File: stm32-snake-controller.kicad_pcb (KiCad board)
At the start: 4 copper layers, 98 x 72 mm, 72 parts, among them J101 Barrel_Jack_MountingPin, J102 JST 2.54 Header, J103 Tag Connector, J301 Conn_01x03, J302 Conn_01x03, J401 Conn_01x07, J402 Conn_01x07, J501 USB_A, Q101 AO3501A, SW101 SW_Push, U101 USBLC6-2SC6, U102 M24C64-RMN, U103 STM32F446RCTx, U201 XC6220B331MR-G, U301 74AHCT1G125, U302 74AHCT1G125, U501 STMPS2141STR, Y101 32.768kHz, Y102 16MHz

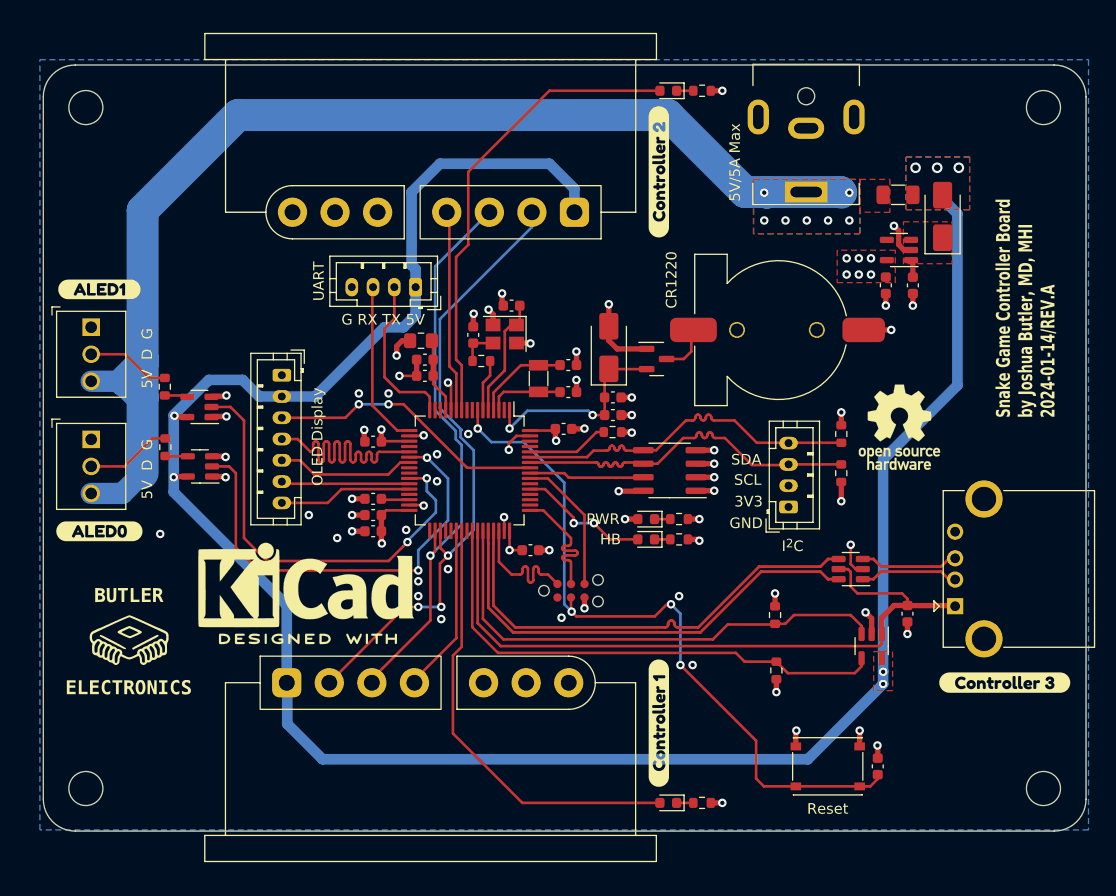
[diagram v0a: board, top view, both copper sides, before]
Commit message: update schematic and pcb design to rev-b
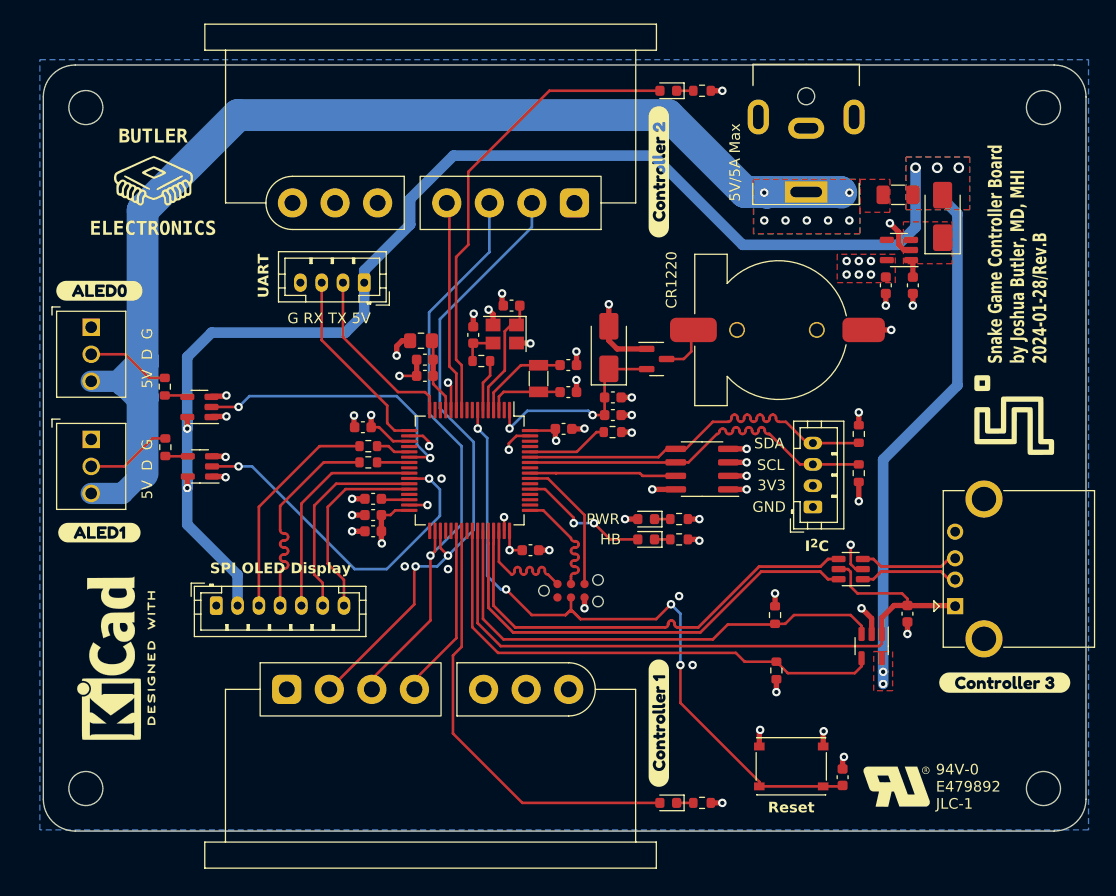
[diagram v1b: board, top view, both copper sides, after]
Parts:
- removed the REF** at (163.7, 112.8)
- removed the REF** at (219.5, 98.0)
- added G***: LOGO, LOGO, F.Cu at (219.2, 131.8)
- added G***: LOGO, LOGO, F.Cu at (230.3, 96.9)
- added R109: 47, Resistor_SMD:R_0603_1608Metric, F.Cu at (169.5, 99.8)
- added R110: 47, Resistor_SMD:R_0603_1608Metric, F.Cu at (169.5, 101.3)
- added REF**: KiCad-Logo2_6mm_SilkScreen, Symbol:KiCad-Logo2_6mm_SilkScreen, F.Cu at (145.2, 119.8)
- D103: value GREEN -> YELLOW
- D104, D105: value GREEN -> BLUE
- moved G*** 43.2 mm to (149.4, 74.9)
- moved kibuzzard-65A37F1A 22.9 mm to (144.3, 108.0)
- moved kibuzzard-65A37F11 22.6 mm to (144.3, 85.2)
- moved OLED102 22.5 mm to (155.3, 114.8), turned to 0 degrees
- moved J102 4.84 mm to (169.2, 84.5)
- moved C110 3.46 mm to (214.1, 130.9)
- moved SW101 3.43 mm to (209.3, 129.9)
- moved U102 3.05 mm to (200.9, 102.0)
- moved OLED101 2.29 mm to (211.3, 105.5)
- moved C104 1.66 mm to (169.0, 98.0)
- moved R107 1.65 mm to (215.6, 98.7)
- moved R108 1.65 mm to (215.6, 102.4)
- moved J402 0.88 mm to (175.3, 77.0)
- moved J401 0.62 mm to (175.5, 122.7)
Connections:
- J401 pad 1: +5V -> +3V3
- J402 pad 1: +5V -> +3V3
- OLED102 pad 3: /MOSI -> Net-(OLED102-SCLK)
- OLED102 pad 4: /SPI_CLK -> Net-(OLED102-MOSI)
- U103 pad 23: /OLED_RST -> /MOSI
- U103 pad 25: unconnected-(U103-PC5-Pad25) -> /OLED_RST
- U103 pad 57: /MOSI -> unconnected-(U103-PB5-Pad57)
- U301 pad 2: /LED_GRID1 -> /LED_GRID0
- U302 pad 2: /LED_GRID0 -> /LED_GRID1
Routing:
- net +5V: track 205.0 -> 169.1 mm
- net /SPI_CLK: track 29.2 -> 3.25 mm
- net /MOSI: track 26.3 -> 3.03 mm, vias 2 -> 0
- net Net-(OLED102-MOSI): track 0.00 -> 21.2 mm
- net Net-(OLED102-SCLK): track 0.00 -> 21.1 mm
- net /LED_GRID0: track 41.8 -> 26.9 mm
- net /OLED_RST: track 13.0 -> 20.9 mm
- net /LED_GRID1: track 40.7 -> 33.3 mm
- net /OLED_CE: track 12.1 -> 19.5 mm
- net /OLED_DC: track 12.5 -> 18.3 mm
- net /~{EEPROM}: track 10.8 -> 13.8 mm
- net /UART_RX: track 15.6 -> 18.1 mm
- net /SDA: track 33.8 -> 36.2 mm
- net /SCL: track 33.8 -> 35.8 mm
- net /SNES_LATCH: track 53.4 -> 55.3 mm
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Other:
- board text added: "${TITLE} by ${COMMENT1} ${ISSUE_DATE}/Rev.${REVISION}"
- board text added: "94V-0 E479892 JLC-1"
- board text added: "SPI OLED Display"
- board text removed: "${TITLE} by ${COMMENT1} ${ISSUE_DATE}/REV.${REVISION}"
- board text removed: "OLED Display"

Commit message: add power switch, rearrange pins for OLED display
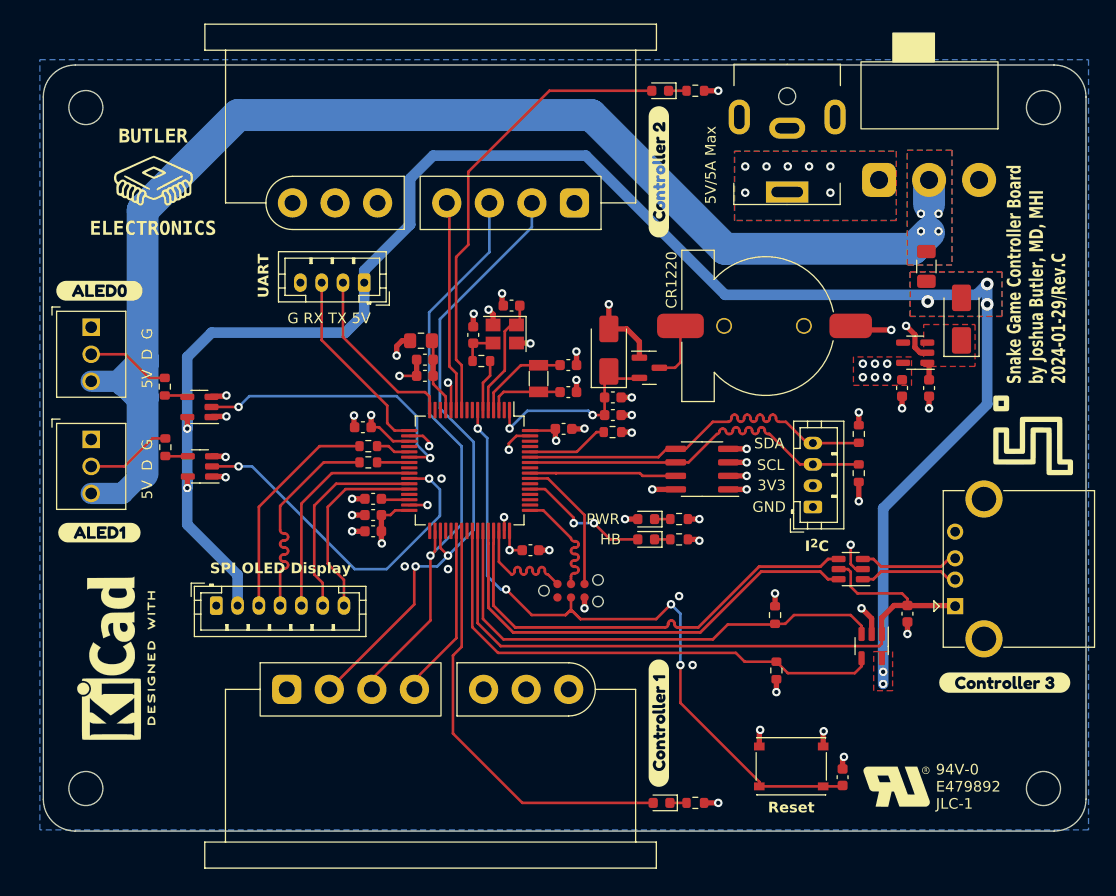
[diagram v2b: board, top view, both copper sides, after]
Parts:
- added SW102: SW_SPDT, User_Footprint:Slide_Switch_SPDT_SS-12D06L5, F.Cu at (222.2, 74.8)
- moved D101 9.81 mm to (225.3, 87.9)
- moved C201 9.77 mm to (222.2, 94.4)
- moved C202 9.77 mm to (219.7, 94.4)
- moved U201 9.77 mm to (220.9, 91.0)
- moved F101 7.24 mm to (222.0, 82.9), turned to -90 degrees
- moved G*** 2.61 mm to (232.0, 98.8)
- moved J101 1.78 mm to (208.9, 80.9)
- moved BT101 1.28 mm to (206.9, 88.5)
- moved Q101 1.07 mm to (196.0, 92.5)
- moved D104 0.76 mm to (197.0, 66.4)
- moved R103 0.63 mm to (200.3, 66.4)
- moved R104 0.63 mm to (200.3, 133.3)
- moved D105 0.63 mm to (197.1, 133.3)
- moved D102 0.25 mm to (192.2, 90.8)
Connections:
- J101 pad 1: VBUS -> Net-(SW102-A)
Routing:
- net VBUS: track 111.1 -> 124.1 mm, vias 7 -> 4
- net +5V: track 169.1 -> 165.2 mm
- net /BAT+: track 4.72 -> 5.62 mm
- net /LED_SNES1: track 44.2 -> 43.5 mm
- net /VBAT: track 19.6 -> 19.0 mm
- net /LED_SNES0: track 41.5 -> 40.9 mm
- net GND: track 69.0 -> 69.5 mm
- net Net-(SW102-A): vias 0 -> 7
- added copper zone on B.Cu, net Net-(SW102-A)
- added copper zone on F.Cu, net Net-(SW102-A)

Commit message: add scoreboard connector
- add ethernet jack for scoreboard connection
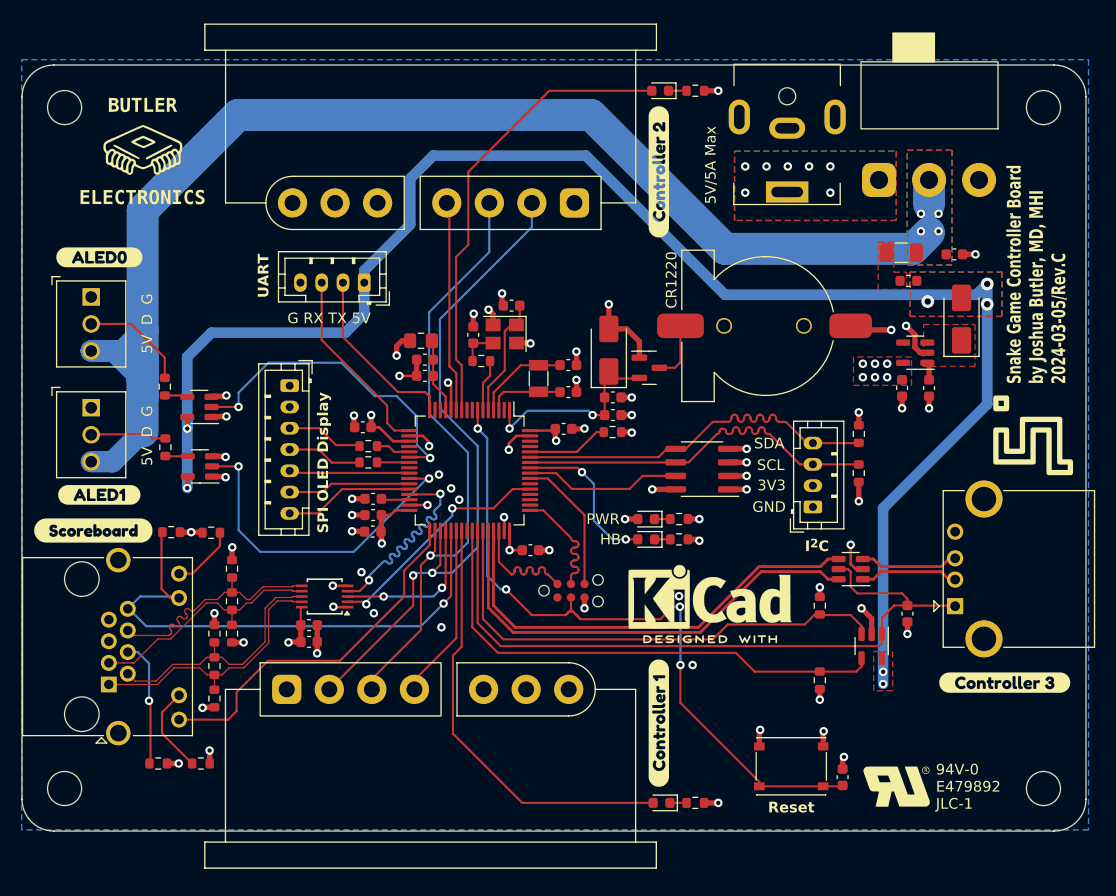
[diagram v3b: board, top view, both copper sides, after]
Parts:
- added C104: 22uF, Capacitor_SMD:C_0603_1608Metric, F.Cu at (224.6, 81.8)
- added C601: 1uF, Capacitor_SMD:C_0603_1608Metric, F.Cu at (164.0, 118.2)
- added C602: 100nF, Capacitor_SMD:C_0603_1608Metric, F.Cu at (164.0, 116.6)
- added J601: 8P8C_LED_Shielded, Connector_RJ:RJ45_Amphenol_RJHSE538X, F.Cu at (145.2, 122.2)
- added L101: L_Ferrite_Small, Inductor_SMD:L_0603_1608Metric, F.Cu at (220.3, 84.3)
- added R601: 10K, Resistor_SMD:R_0603_1608Metric, F.Cu at (151.0, 107.9)
- added R602: 1K5, Resistor_SMD:R_0603_1608Metric, F.Cu at (153.8, 129.6)
- added R603: 1K5, Resistor_SMD:R_0603_1608Metric, F.Cu at (154.8, 108.0)
- added R604: 470, Resistor_SMD:R_0603_1608Metric, F.Cu at (155.1, 117.4)
- added R605: 470, Resistor_SMD:R_0603_1608Metric, F.Cu at (156.7, 117.4)
- added R606: 140, Resistor_SMD:R_0603_1608Metric, F.Cu at (155.1, 120.5)
- added R607: 140, Resistor_SMD:R_0603_1608Metric, F.Cu at (156.7, 114.4)
- added R608: 470, Resistor_SMD:R_0603_1608Metric, F.Cu at (155.1, 123.5)
- added R609: 470, Resistor_SMD:R_0603_1608Metric, F.Cu at (156.7, 111.3)
- added R610: 10K, Resistor_SMD:R_0603_1608Metric, F.Cu at (149.8, 129.6)
- added U601: PCA9615DP, Package_SO:TSSOP-10_3x3mm_P0.5mm, F.Cu at (165.4, 114.0)
- added kibuzzard-65E6C2BD: G***, kibuzzard-65E6C2BD, F.Cu at (143.7, 107.8)
- moved REF** 56.8 mm to (201.7, 114.0), turned to 0 degrees
- moved OLED101 21.8 mm to (162.2, 94.1), turned to -90 degrees
- moved R502 4.30 mm to (212.0, 114.8)
- moved R501 4.18 mm to (212.0, 121.8)
- moved kibuzzard-65A37F1A 3.55 mm to (144.3, 104.4)
- moved kibuzzard-65A37F11 3.14 mm to (144.3, 82.1)
- moved G*** 3.06 mm to (148.4, 72.0)
- moved J302 2.97 mm to (143.5, 98.7)
- moved J301 2.85 mm to (143.5, 88.3)
- moved F101 2.68 mm to (219.7, 81.6), turned to 180 degrees
- moved H101 2.00 mm to (141.0, 68.0)
- moved H104 2.00 mm to (141.0, 132.0)
- renumbered C111 to C101, C114 to C102, C110 to C103, C112 to C105, C113 to C106, C103 to C107, C104 to C109, C109 to C110, C105 to C111, C106 to C112, C107 to C113, C115 to C114, C101 to C115, C102 to C116, D103 to D102, D104 to D103, D105 to D104, D106 to D105, D102 to D106, H103 to H102, H102 to H103, J103 to J102, J102 to J103, OLED102 to OLED101, R106 to R101, R110 to R102, R109 to R103, R107 to R104, R101 to R105, R103 to R106, R104 to R107, R105 to R108, R108 to R109, R102 to R110, R502 to R501, R501 to R502, SW102 to SW101, SW101 to SW102
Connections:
- F101 pad 2: +5V -> Net-(F101-Pad2)
- OLED101 pad 2: +5V -> +3V3
- U103 pad 29: unconnected-(U103-PB10-Pad29) -> /SB_SCL
- U103 pad 33: unconnected-(U103-PB12-Pad33) -> /I2C_LED
- U103 pad 36: unconnected-(U103-PB15-Pad36) -> /SB_EN
- U103 pad 37: unconnected-(U103-PC6-Pad37) -> /SB_LINK
- U103 pad 53: /LED_HB -> /SB_SDA
- U103 pad 57: unconnected-(U103-PB5-Pad57) -> /LED_HB
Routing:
- net /SB_LINK: track 0.00 -> 51.1 mm, vias 0 -> 1
- net /I2C_LED: track 0.00 -> 34.2 mm
- net /scoreboard/SDA_N: track 0.00 -> 25.2 mm
- net /scoreboard/SDA_P: track 0.00 -> 23.7 mm
- net /scoreboard/SCL_P: track 0.00 -> 23.0 mm
- net /scoreboard/SCL_N: track 0.00 -> 22.9 mm
- net /SB_SDA: track 0.00 -> 22.3 mm, vias 0 -> 2
- net /SB_SCL: track 0.00 -> 22.0 mm, vias 0 -> 2
- net /SB_EN: track 0.00 -> 14.7 mm, vias 0 -> 2
- net +5V: track 165.2 -> 150.9 mm
- net Net-(OLED101-MOSI): track 21.2 -> 7.09 mm
- net Net-(OLED101-SCLK): track 21.1 -> 7.26 mm
- net Net-(J601-Pad4): track 0.00 -> 11.9 mm, vias 0 -> 1
- net +3V3: track 35.8 -> 46.6 mm, vias 18 -> 24
- net /OLED_RST: track 20.9 -> 11.3 mm
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- added copper zone on F.Cu, net Net-(F101-Pad2)
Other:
- board size 98 x 72 mm -> 100 x 72 mm

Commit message: remove pull-down resistor
- The original schematic had pull-down resistors for link detection, after a breadboard testing, it failed. Looked at the oscilloscope, it showed that the signal voltage dropped,  acting like a voltage divider so the line did not get pulled down to 0V. Removing the resistor fixed that.
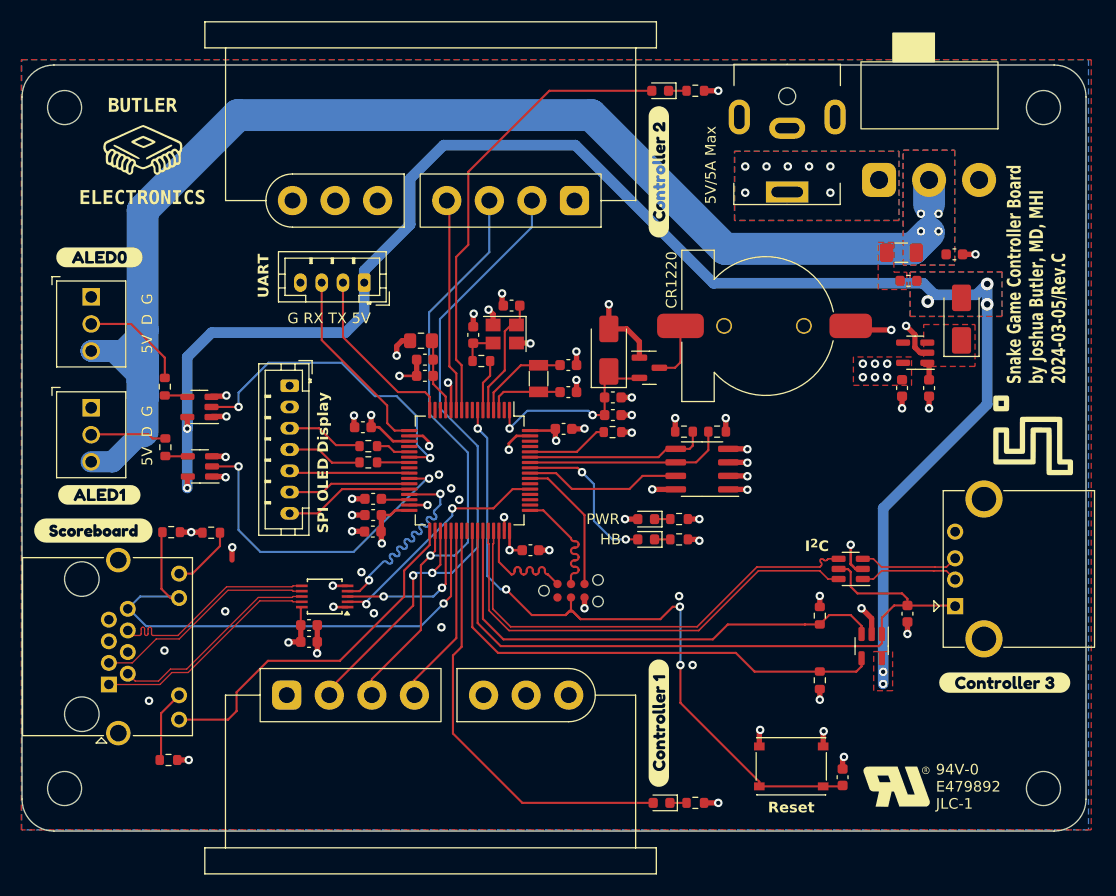
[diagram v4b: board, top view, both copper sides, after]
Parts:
- removed the OLED101 at (211.3, 105.5)
- removed R604, R605, R608, R609: 470, Resistor_SMD:R_0603_1608Metric
- removed R606, R607: 140, Resistor_SMD:R_0603_1608Metric
- removed R610: 10K, Resistor_SMD:R_0603_1608Metric
- removed REF**: KiCad-Logo2_6mm_SilkScreen, Symbol:KiCad-Logo2_6mm_SilkScreen
- moved R104 16.4 mm to (199.2, 98.5), turned to 180 degrees
- moved R109 13.9 mm to (202.3, 98.5), turned to 0 degrees
- moved R602 3.07 mm to (150.8, 129.3)
- moved R502 0.94 mm to (212.0, 115.8)
- moved J401 0.54 mm to (175.5, 123.2)
- moved J402 0.22 mm to (175.3, 76.7)
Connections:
- J601 pad 4: Net-(J601-Pad4) -> GND
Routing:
- net /SDA: track 36.2 -> 17.1 mm
- net /SCL: track 35.8 -> 19.0 mm
- net Net-(J601-Pad4): track 11.9 -> 0.00 mm, vias 1 -> 0
- net /scoreboard/SDA_P: track 23.7 -> 19.9 mm
- net /scoreboard/SDA_N: track 25.2 -> 21.4 mm
- net +3V3: track 46.6 -> 44.0 mm, vias 24 -> 22
- net /scoreboard/SCL_P: track 23.0 -> 21.0 mm
- net /scoreboard/SCL_N: track 22.9 -> 21.0 mm
- net Net-(J601-Pad10): track 8.25 -> 6.84 mm
- net GND: track 78.2 -> 77.0 mm, vias 58 -> 59
- net +5V: track 150.9 -> 151.8 mm
- net /SNES_LATCH: track 57.2 -> 57.9 mm
- net /SNES_CLK: track 62.8 -> 63.6 mm
- net /USB_D_P: track 8.73 -> 9.34 mm
- net /USB_D_N: track 8.73 -> 9.34 mm
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- added copper zone on F.Cu, net GND
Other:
- board text added: "0"
- board text added: "0 mm"
- board text added: "0.0152 mm"
- board text added: "0.02"
- board text added: "0.02032 mm"
- board text added: "0.035 mm"
- board text added: "0.0900 mm / 0.0900 mm"
- board text added: "0.0994 mm"
- board text added: "0.2000 mm"
- board text added: "1"
- board text added: "1.265 mm"
- board text added: "1.6268 mm"
- board text added: "100.0000 mm x 72.0000 mm"
- board text added: "3.3"
- board text added: "4"
- board text added: "4.6"
- board text added: "B.Cu"
- board text added: "B.Mask"
- board text added: "B.Paste"
- board text added: "B.Silkscreen"
- board text added: "BOARD CHARACTERISTICS"
- board text added: "Black"
- board text added: "Board Thickness:"
- board text added: "Board overall dimensions:"
- board text added: "Bottom Silk Screen"
- board text added: "Bottom Solder Mask"
- board text added: "Bottom Solder Paste"
- board text added: "Castellated pads:"
- board text added: "Color"
- board text added: "Copper Finish:"
- board text added: "Copper Layer Count:"
- board text added: "Dielectric 1"
- board text added: "Dielectric 2"
- board text added: "Dielectric 3"
- board text added: "Edge card connectors:"
- board text added: "Epsilon R"
- board text added: "F.Cu"
- board text added: "F.Mask"
- board text added: "F.Paste"
- board text added: "F.Silkscreen"
- board text added: "FR4"
- board text added: "FR4 natural"
- board text added: "HAL SnPb"
- board text added: "Impedance Control:"
- board text added: "Impedance Notes: Board: JLC04161H-3313 D_P and D_N pairs: 90 ohms (0.1554 width/0.2032 spacing) SDA_P and SDA_N: 100 ohms (0.1217 width/0.2032 spacing) SCL_P and SCL_N: 100 ohms (0.1217 width/0.2032 spacing)"
- board text added: "In1.Cu"
- board text added: "In2.Cu"
- board text added: "Layer Name"
- board text added: "Loss Tangent"
- board text added: "Material"
- board text added: "Min hole diameter:"
- board text added: "Min track/spacing:"
- board text added: "No"
- board text added: "Not specified"
- board text added: "PCB Stackup: JLC04161H-3313"
- board text added: "Plated Board Edge:"
- board text added: "Thickness (mm)"
- board text added: "Top Silk Screen"
- board text added: "Top Solder Mask"
- board text added: "Top Solder Paste"
- board text added: "Type"
- board text added: "White"
- board text added: "Yes"
- board text added: "copper"
- board text added: "core"
- board text added: "prepreg"
- board text removed: "3V3"
- board text removed: "GND"
- board text removed: "SCL"
- board text removed: "SDA"
